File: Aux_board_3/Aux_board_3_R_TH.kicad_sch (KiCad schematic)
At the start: 40 parts, among them Q1 BSS138KJ, Q10 BSS84KJ, Q11 BSS138KJ, Q12 BSS84KJ, Q13 BSS138KJ, Q14 BSS84KJ, Q15 BSS138KJ, Q16 BSS84KJ, Q2 BSS84KJ, Q3 BSS138KJ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

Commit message: Board 3 layout started
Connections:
- net R_HOME: no longer R28.2
- net R_LIM_MAX_IN: no longer names the net of R25.2
- net R_LIM_MIN_IN: no longer names the net of R22.2
- net TH_ENC_A: no longer names the net of Q8.2 (S), R33.1
- net TH_ENC_A_IN: no longer names the net of R31.2
- net TH_ENC_B: no longer names the net of Q10.2 (S), R36.1
- net TH_ENC_B_IN: no longer names the net of R34.2
- net TH_HOME: no longer names the net of Q16.2 (S), R45.1
- net TH_HOME_IN: no longer names the net of R43.2
- net TH_LIM_MAX: no longer names the net of Q14.2 (S), R42.1
- net TH_LIM_MAX_IN: no longer names the net of R40.2
- net TH_LIM_MIN: no longer names the net of Q12.2 (S), R39.1
- net TH_LIM_MIN_IN: no longer names the net of R37.2

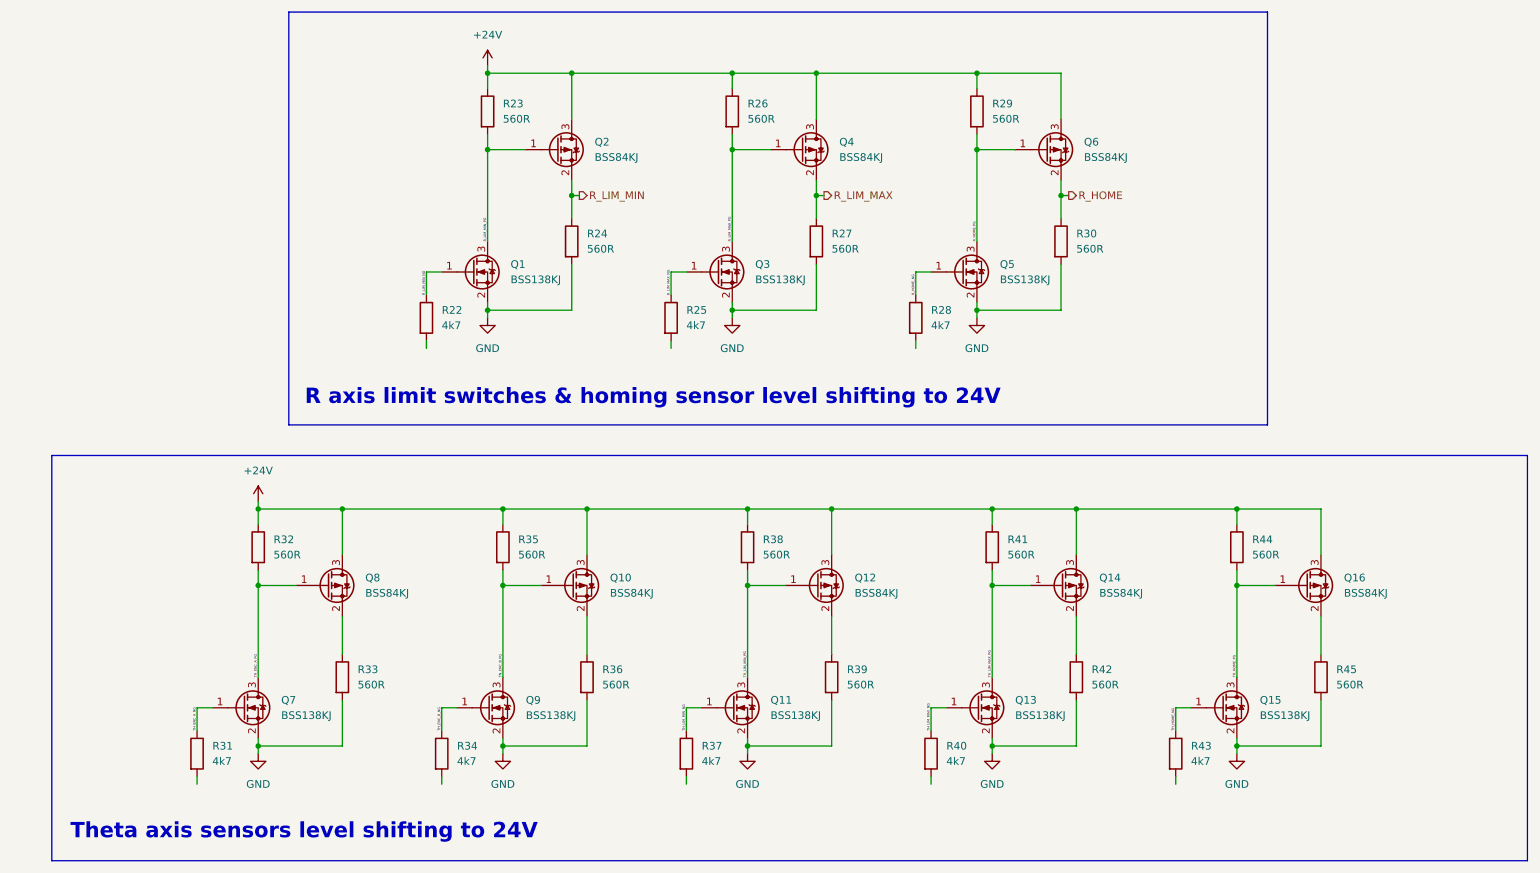
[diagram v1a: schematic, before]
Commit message: Board 3 MODBUS and servos done
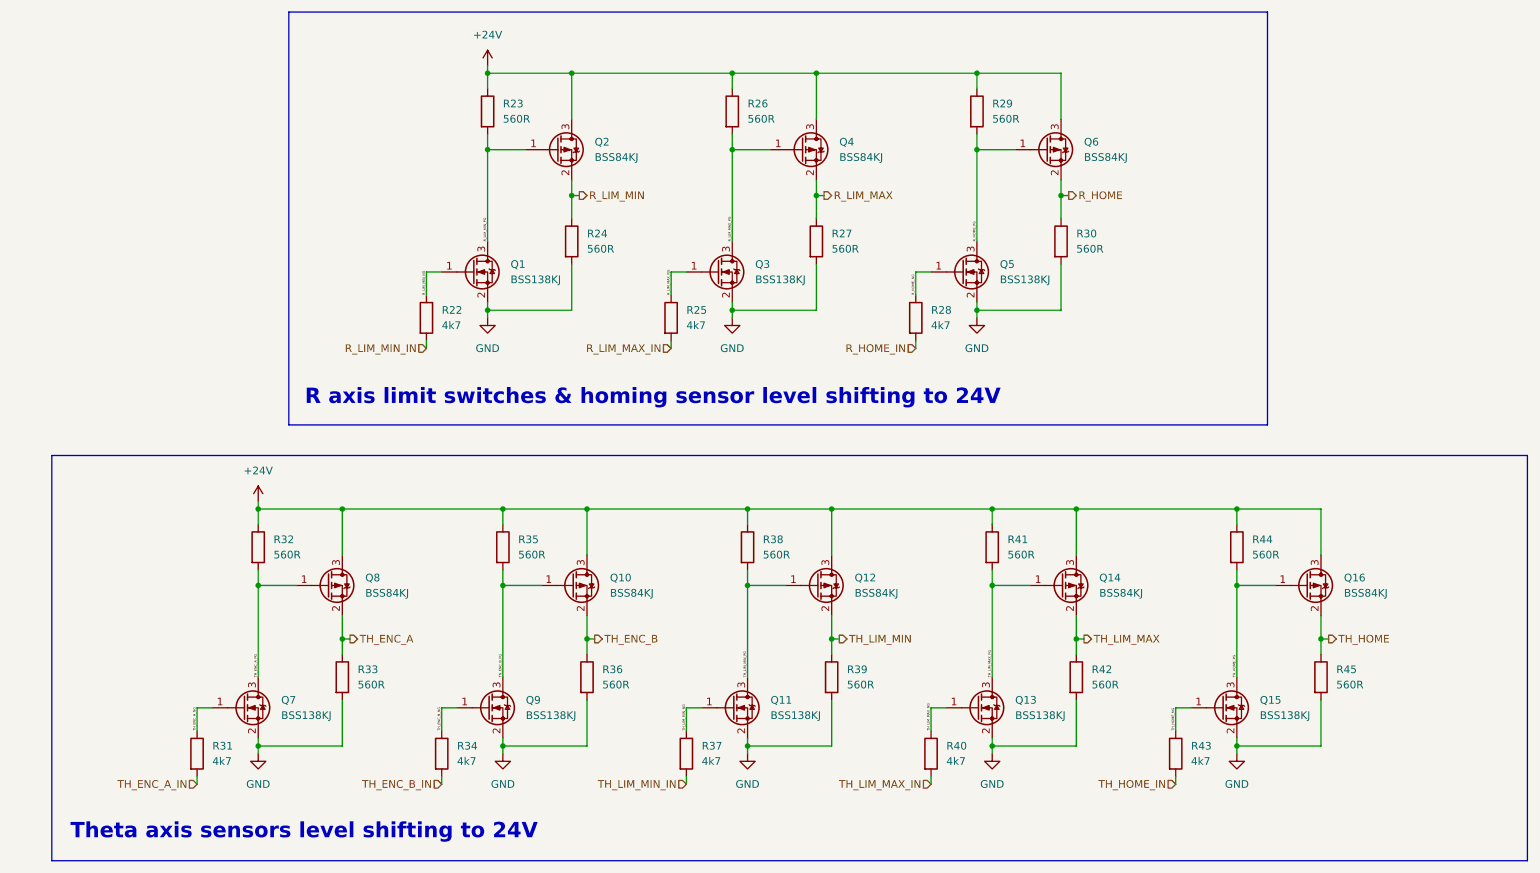
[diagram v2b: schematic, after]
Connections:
- net R_LIM_MAX_IN: now reaches R25.2
- net TH_ENC_A_IN: now reaches R31.2
- net TH_ENC_A: now reaches Q8.2 (S), R33.1
- net TH_LIM_MIN_IN: now reaches R37.2
- net TH_HOME: now reaches Q16.2 (S), R45.1
- net TH_ENC_B: now reaches Q10.2 (S), R36.1
- net TH_LIM_MIN: now reaches Q12.2 (S), R39.1
- net TH_LIM_MAX_IN: now reaches R40.2
- net TH_ENC_B_IN: now reaches R34.2
- net TH_HOME_IN: now reaches R43.2
- net TH_LIM_MAX: now reaches Q14.2 (S), R42.1
- net R_LIM_MIN_IN: now reaches R22.2
- net R_HOME_IN: now reaches R28.2
